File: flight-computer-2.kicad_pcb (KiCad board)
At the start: 4 copper layers, 51 x 51 mm, 79 parts, among them J1 USB4105-GF-A, J2 THR, J3 SER1, J4 SER2, J5 SER3, J6 SER4, J7 Breakout, SW1 RESET, SW2 BOOT, U1 AP2114H-3.3TRG1, U2 MUN5214DW1T1G, U3 BNO080, U4 CP2102N, U5 MPL3115A2, U6 ESP32-PICO-D4, Y1 32.768kHz

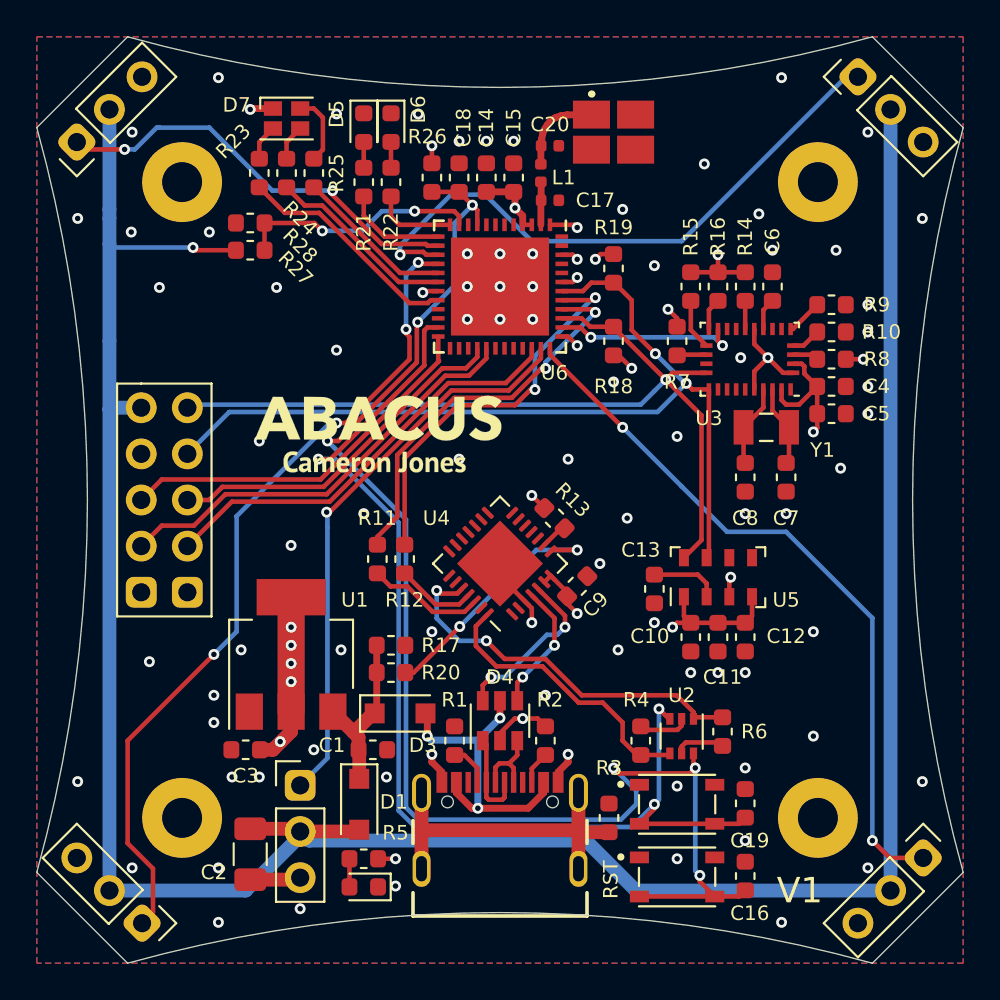
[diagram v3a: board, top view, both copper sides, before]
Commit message: New power filtering cap and minor routing adjustments
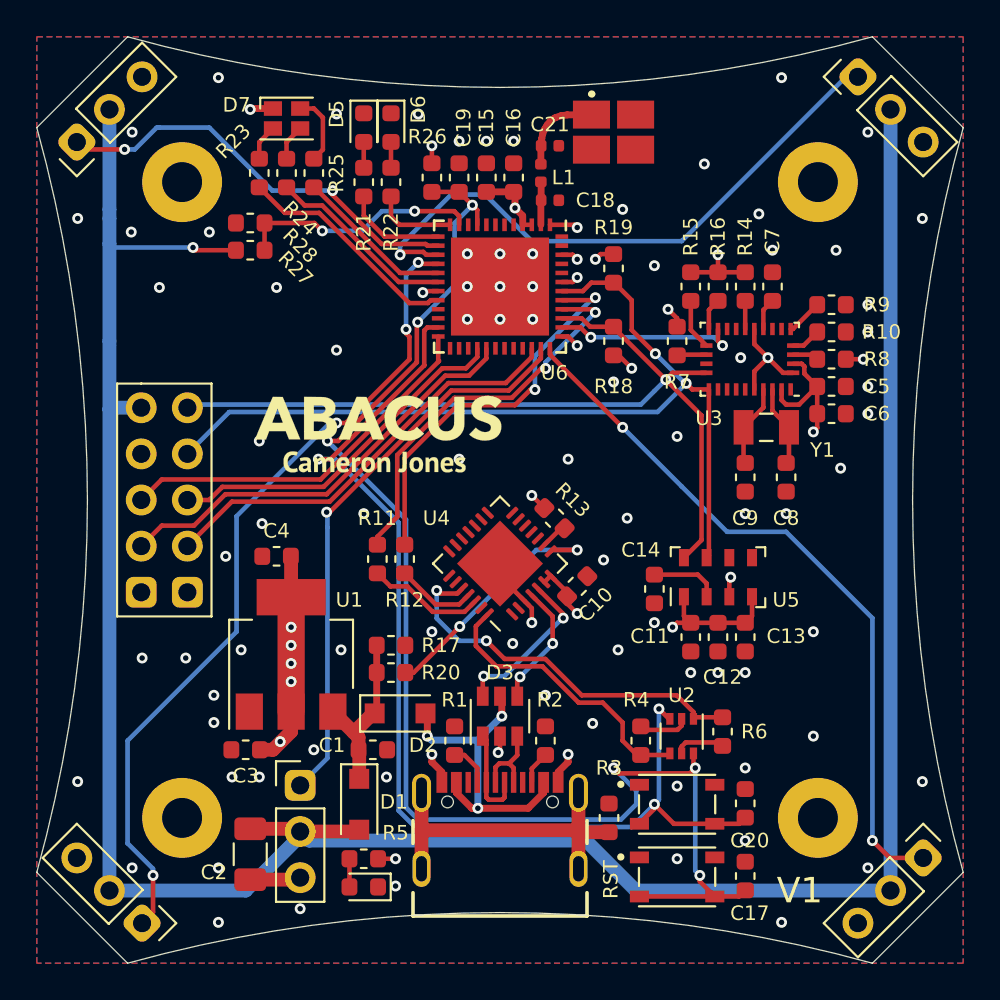
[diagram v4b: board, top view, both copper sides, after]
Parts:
- removed the D4 at (117.5, 79.7)
- added C4: 10uF, Capacitor_SMD:C_0603_1608Metric, F.Cu at (105.2, 70.6)
- added D3: USBLC6-2SC6, Package_TO_SOT_SMD:SOT-23-6, F.Cu at (117.5, 79.4)
- renumbered C9 to C10, C10 to C11, C11 to C12, C12 to C13, C13 to C14, C14 to C15, C15 to C16, C16 to C17, C17 to C18, C18 to C19, C19 to C20, C20 to C21, C4 to C5, C5 to C6, C6 to C7, C7 to C8, C8 to C9, D3 to D2, D2 to D4
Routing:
- net GND: track 20.5 -> 18.0 mm, vias 85 -> 89
- net +3V3: track 50.9 -> 53.1 mm
- net Net-(D3-Pad1): track 5.14 -> 5.67 mm

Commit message: Removing programming selector resistors
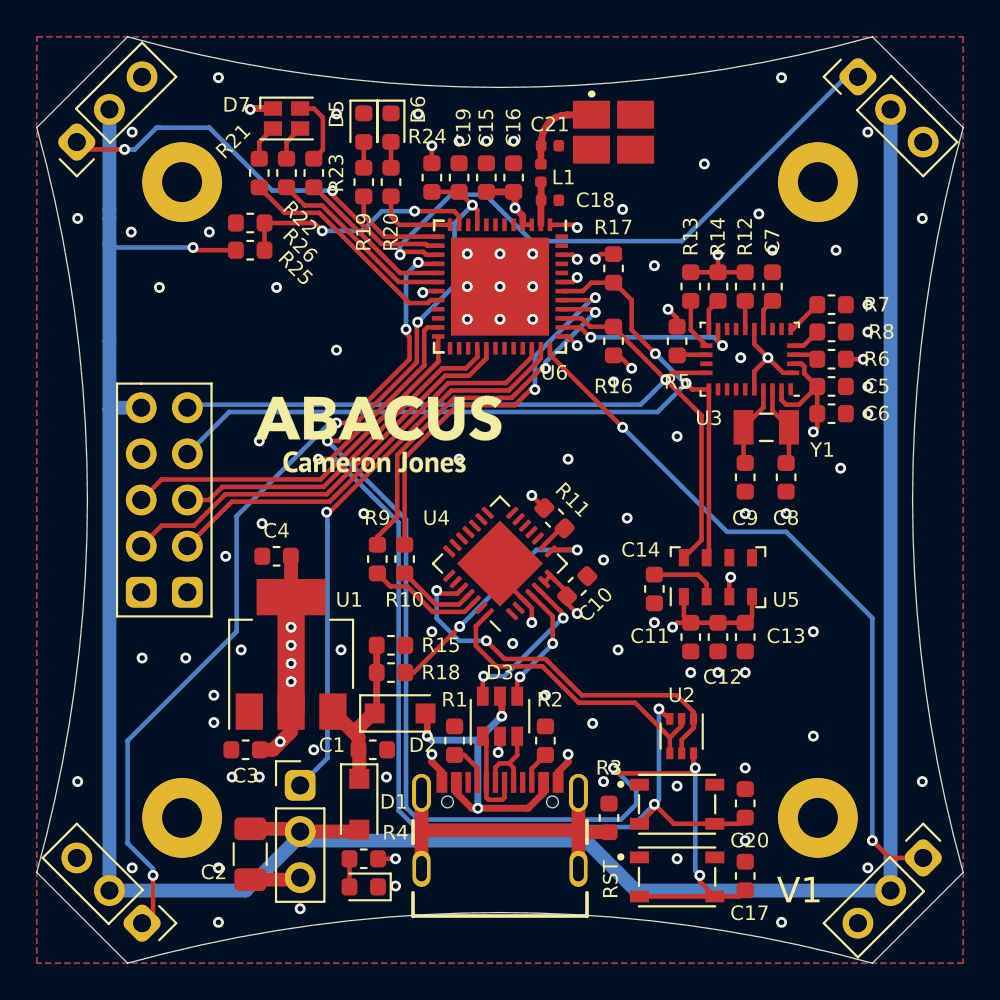
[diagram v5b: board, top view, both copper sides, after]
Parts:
- removed the R4 at (125.2, 80.8)
- removed the R6 at (129.8, 80.2)
- renumbered R12 to R10, R13 to R11, R14 to R12, R15 to R13, R16 to R14, R17 to R15, R18 to R16, R19 to R17, R20 to R18, R21 to R19, R22 to R20, R23 to R21, R24 to R22, R25 to R23, R26 to R24, R27 to R25, R28 to R26, R5 to R4, R7 to R5, R8 to R6, R9 to R7, R10 to R8, R11 to R9
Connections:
- U2 pad 2: Net-(R4-Pad1) -> /DTR
- U2 pad 5: Net-(R6-Pad2) -> /RTS
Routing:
- net Net-(R6-Pad2): track 2.80 -> 0.00 mm
- net Net-(R4-Pad1): track 2.80 -> 0.00 mm
- net /DTR: track 15.8 -> 16.9 mm
- net /RTS: track 21.4 -> 22.0 mm
- net GND: vias 89 -> 90

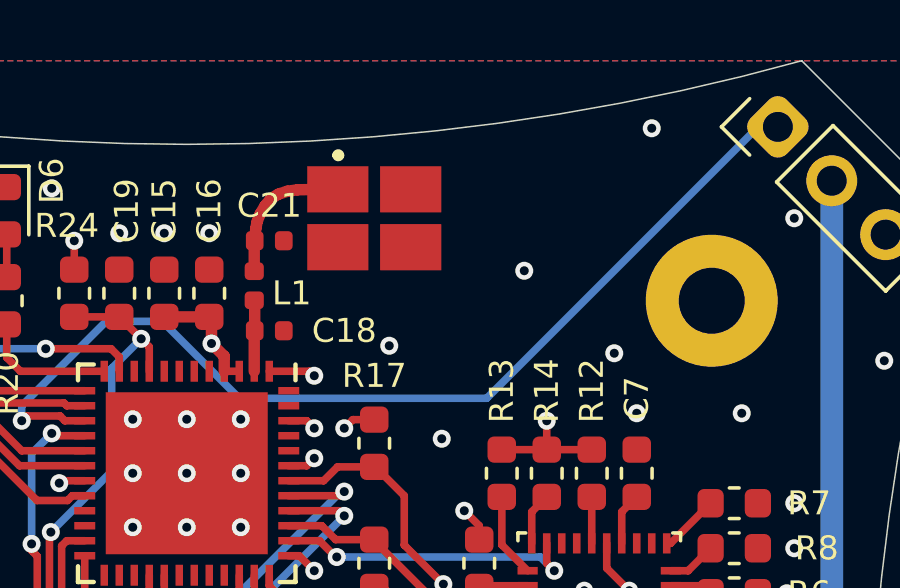
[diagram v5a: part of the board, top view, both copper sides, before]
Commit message: More vias near antenna pads
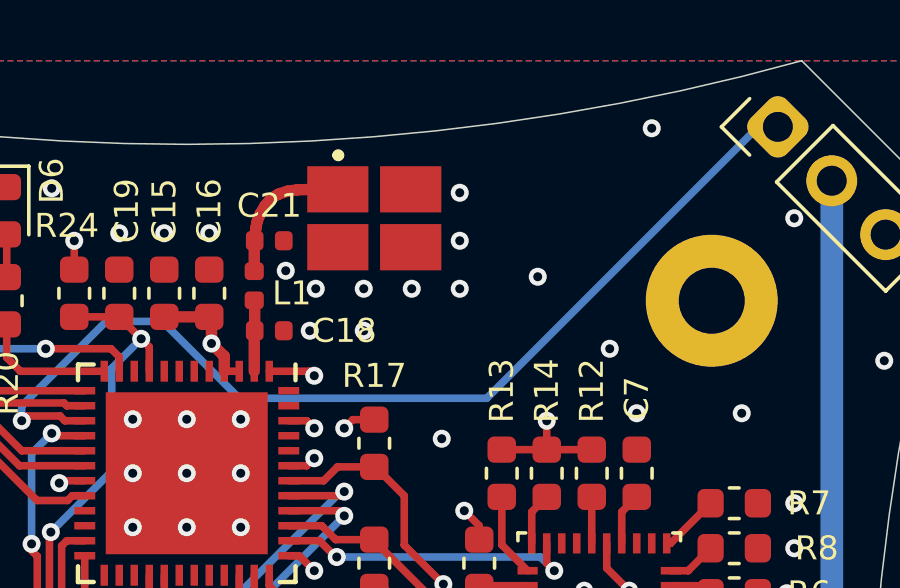
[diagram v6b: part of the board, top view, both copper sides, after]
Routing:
- net GND: vias 90 -> 98
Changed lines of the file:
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@@
     (thickness 1.6)
     (drawings 16)
-    (tracks 654)
+    (tracks 662)
     (zones 0)
     (modules 78)
@@
   (segment (start 121.25 81.924264) (end 120.7 82.474264) (width 0.381) (layer F.Cu) (net 1) (status 20))
   (segment (start 121.25 81.5) (end 121.25 81.924264) (width 0.381) (layer F.Cu) (net 1))
-  (via (at 124.25 51.5) (size 0.6) (drill 0.3) (layers F.Cu B.Cu) (net 1))
-  (via (at 128.75 49) (size 0.6) (drill 0.3) (layers F.Cu B.Cu) (net 1))
-  (via (at 131.75 51.75) (size 0.6) (drill 0.3) (layers F.Cu B.Cu) (net 1))
+  (via (at 129.2 49.2) (size 0.6) (drill 0.3) (layers F.Cu B.Cu) (net 1))
+  (via (at 131.6 51.6) (size 0.6) (drill 0.3) (layers F.Cu B.Cu) (net 1))
   (via (at 136 53.75) (size 0.6) (drill 0.3) (layers F.Cu B.Cu) (net 1))
   (via (at 136.25 65.75) (size 0.6) (drill 0.3) (layers F.Cu B.Cu) (net 1))
@@
   (via (at 122.6 79.8) (size 0.6) (drill 0.3) (layers F.Cu B.Cu) (net 1))
   (via (at 123.2 83) (size 0.6) (drill 0.3) (layers F.Cu B.Cu) (net 1))
+  (via (at 126.6 48) (size 0.6) (drill 0.3) (layers F.Cu B.Cu) (net 1))
+  (via (at 126.6 46.4) (size 0.6) (drill 0.3) (layers F.Cu B.Cu) (net 1))
+  (via (at 123.4 51) (size 0.6) (drill 0.3) (layers F.Cu B.Cu) (net 1))
+  (via (at 120.8 49) (size 0.6) (drill 0.3) (layers F.Cu B.Cu) (net 1))
+  (via (at 121.6 51) (size 0.6) (drill 0.3) (layers F.Cu B.Cu) (net 1))
+  (via (at 126.6 49.6) (size 0.6) (drill 0.3) (layers F.Cu B.Cu) (net 1))
+  (via (at 125 49.6) (size 0.6) (drill 0.3) (layers F.Cu B.Cu) (net 1))
+  (via (at 123.4 49.6) (size 0.6) (drill 0.3) (layers F.Cu B.Cu) (net 1))
+  (via (at 121.8 49.6) (size 0.6) (drill 0.3) (layers F.Cu B.Cu) (net 1))
   (segment (start 119.75 49.015) (end 119.75 48.015) (width 0.381) (layer F.Cu) (net 2) (status 30))
   (segment (start 119.765 48) (end 119.8 47.6) (width 0.381) (layer F.Cu) (net 2) (status 10))

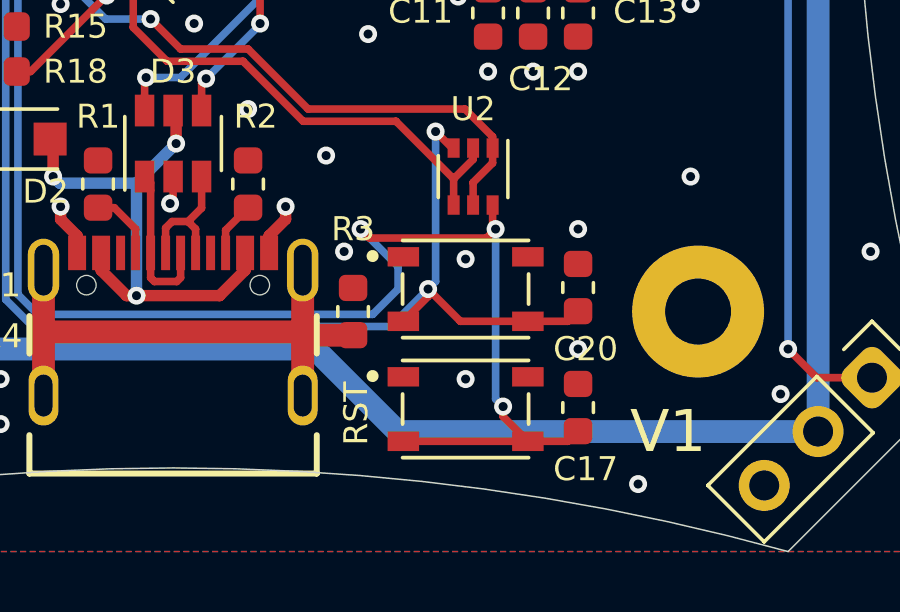
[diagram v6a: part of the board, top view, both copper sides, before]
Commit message: Added MPNs for passives and modified SW symbols
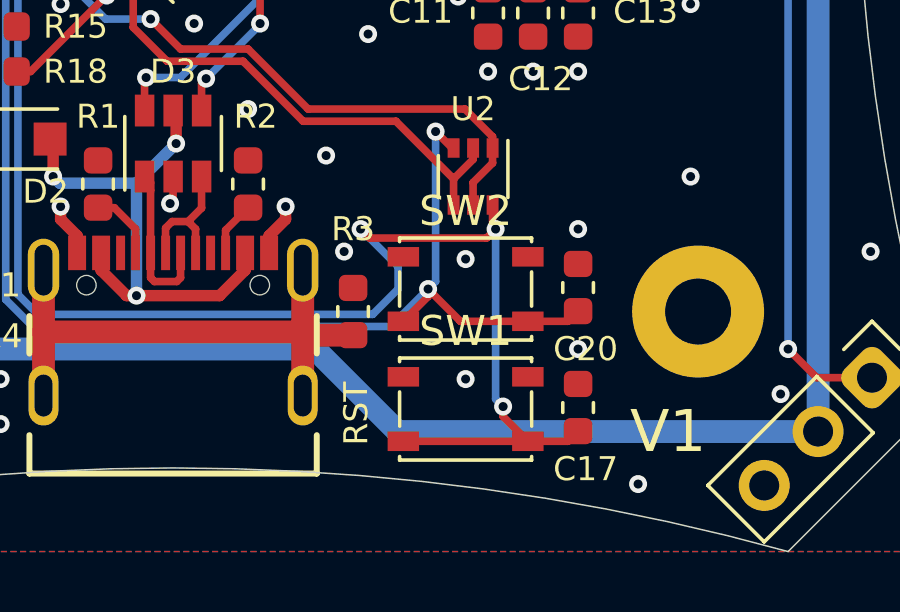
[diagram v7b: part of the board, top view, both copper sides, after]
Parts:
- D4: value LTST-C191KGKT -> Green
- SW1, SW2: footprint flight-computer-2:SW_PTS810_SJM_250_SMTR_LFS -> Button_Switch_SMD:SW_SPST_PTS810
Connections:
- SW1 pad 2: GND -> /EN
- SW2 pad 2: GND -> /IO0

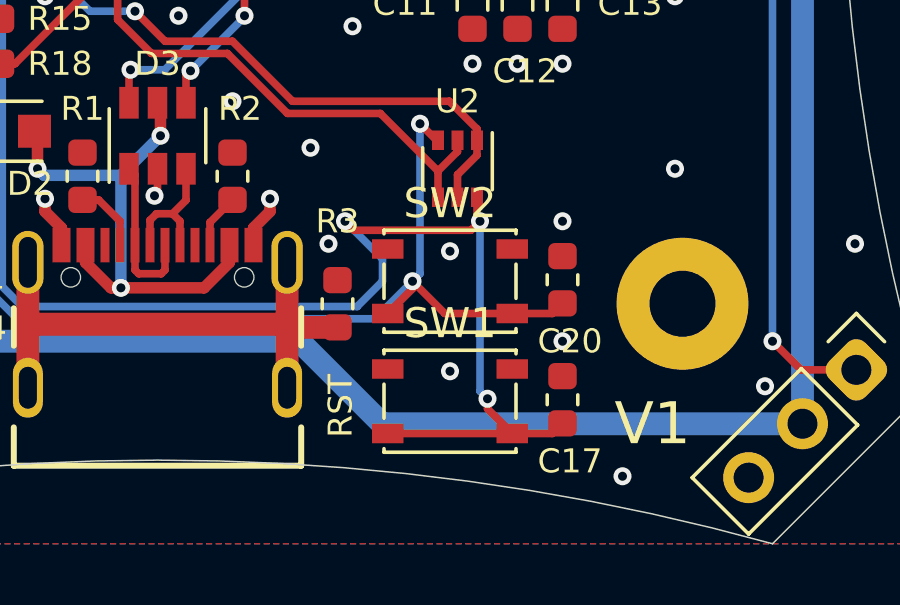
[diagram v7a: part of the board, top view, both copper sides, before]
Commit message: Readded 3D model for buttons
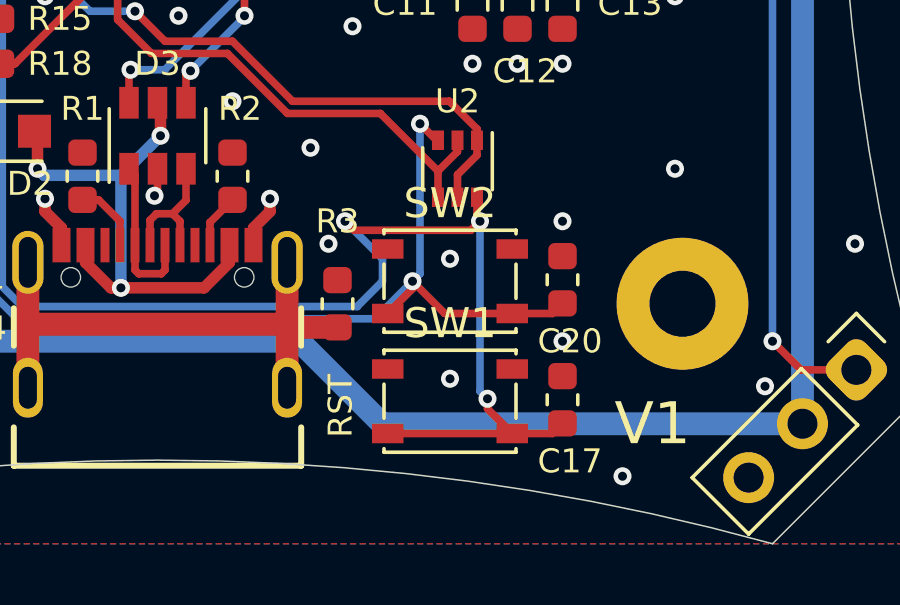
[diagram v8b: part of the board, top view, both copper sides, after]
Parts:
- SW1, SW2: footprint Button_Switch_SMD:SW_SPST_PTS810 -> flight-computer-2:SW_SPST_PTS810
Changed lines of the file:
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@@
     )
   )
-  (module Button_Switch_SMD:SW_SPST_PTS810 (layer F.Cu)
+  (module flight-computer-2:SW_SPST_PTS810 (layer F.Cu)
     (at 127.25 88.25)
     (descr "C&K Components, PTS 810 Series, Microminiature SMT Top Actuated, http://www.ckswitches.com/media/1476/pts810.pdf")
@@
     (fp_text value RESET (at 0 2.6) (layer F.Fab)
       (effects (font (size 1 1) (thickness 0.15)))
-    )
-    (fp_arc (start 0.4 0) (end 0.4 -1.1) (angle 180) (layer F.Fab) (width 0.1))
-    (fp_arc (start -0.4 0) (end -0.4 1.1) (angle 180) (layer F.Fab) (width 0.1))
-    (fp_text user %R (at 0 0) (layer F.Fab)
-      (effects (font (size 0.6 0.6) (thickness 0.09)))
     )
     (fp_line (start -2.85 -1.85) (end 2.85 -1.85) (layer F.CrtYd) (width 0.05))
@@
     (fp_line (start 2.1 -1.6) (end -2.1 -1.6) (layer F.Fab) (width 0.1))
     (fp_line (start 2.1 1.6) (end 2.1 -1.6) (layer F.Fab) (width 0.1))
+    (fp_arc (start 0.4 0) (end 0.4 -1.1) (angle 180) (layer F.Fab) (width 0.1))
+    (fp_arc (start -0.4 0) (end -0.4 1.1) (angle 180) (layer F.Fab) (width 0.1))
+    (fp_text user %R (at 0 0) (layer F.Fab)
+      (effects (font (size 0.6 0.6) (thickness 0.09)))
+    )
     (pad 2 smd rect (at 2.075 1.075) (size 1.05 0.65) (layers F.Cu F.Paste F.Mask)
       (net 5 /EN))
@@
     (pad 1 smd rect (at -2.075 -1.075) (size 1.05 0.65) (layers F.Cu F.Paste F.Mask)
       (net 1 GND))
-    (model ${KISYS3DMOD}/Button_Switch_SMD.3dshapes/SW_SPST_PTS810.wrl
+    (model ${KIPRJMOD}/3d/SW_PTS810_SJM_250_SMTR_LFS.stp
       (at (xyz 0 0 0))
       (scale (xyz 1 1 1))
-      (rotate (xyz 0 0 0))
+      (rotate (xyz -90 0 0))
     )
   )
-  (module Button_Switch_SMD:SW_SPST_PTS810 (layer F.Cu)
+  (module flight-computer-2:SW_SPST_PTS810 (layer F.Cu)
     (at 127.25 84.25)
     (descr "C&K Components, PTS 810 Series, Microminiature SMT Top Actuated, http://www.ckswitches.com/media/1476/pts810.pdf")
@@
       (effects (font (size 1 1) (thickness 0.15)))
     )
+    (fp_text user %R (at 0 0) (layer F.Fab)
+      (effects (font (size 0.6 0.6) (thickness 0.09)))
+    )
+    (fp_arc (start -0.4 0) (end -0.4 1.1) (angle 180) (layer F.Fab) (width 0.1))
+    (fp_arc (start 0.4 0) (end 0.4 -1.1) (angle 180) (layer F.Fab) (width 0.1))
     (fp_line (start 2.1 1.6) (end 2.1 -1.6) (layer F.Fab) (width 0.1))
     (fp_line (start 2.1 -1.6) (end -2.1 -1.6) (layer F.Fab) (width 0.1))
@@
     (fp_line (start -2.85 1.85) (end -2.85 -1.85) (layer F.CrtYd) (width 0.05))
     (fp_line (start -2.85 -1.85) (end 2.85 -1.85) (layer F.CrtYd) (width 0.05))
-    (fp_text user %R (at 0 0) (layer F.Fab)
-      (effects (font (size 0.6 0.6) (thickness 0.09)))
-    )
-    (fp_arc (start -0.4 0) (end -0.4 1.1) (angle 180) (layer F.Fab) (width 0.1))
-    (fp_arc (start 0.4 0) (end 0.4 -1.1) (angle 180) (layer F.Fab) (width 0.1))
     (pad 1 smd rect (at -2.075 -1.075) (size 1.05 0.65) (layers F.Cu F.Paste F.Mask)
       (net 1 GND))
@@
     (pad 2 smd rect (at 2.075 1.075) (size 1.05 0.65) (layers F.Cu F.Paste F.Mask)
       (net 6 /IO0))
-    (model ${KISYS3DMOD}/Button_Switch_SMD.3dshapes/SW_SPST_PTS810.wrl
+    (model ${KIPRJMOD}/3d/SW_PTS810_SJM_250_SMTR_LFS.stp
       (at (xyz 0 0 0))
       (scale (xyz 1 1 1))
-      (rotate (xyz 0 0 0))
+      (rotate (xyz -90 0 0))
     )
   )
@@
   (via (at 113.75 81.5) (size 0.6) (drill 0.3) (layers F.Cu B.Cu) (net 1))
   (via (at 111.75 88.75) (size 0.6) (drill 0.3) (layers F.Cu B.Cu) (net 1))
-  (via (at 127.25 87.25) (size 0.6) (drill 0.3) (layers F.Cu B.Cu) (net 1))
-  (via (at 127.25 83.25) (size 0.6) (drill 0.3) (layers F.Cu B.Cu) (net 1))
+  (via (at 127.25 87.5) (size 0.6) (drill 0.3) (layers F.Cu B.Cu) (net 1))
+  (via (at 127.25 83.5) (size 0.6) (drill 0.3) (layers F.Cu B.Cu) (net 1))
   (via (at 131 82.25) (size 0.6) (drill 0.3) (layers F.Cu B.Cu) (net 1))
   (via (at 131 86.25) (size 0.6) (drill 0.3) (layers F.Cu B.Cu) (net 1))
